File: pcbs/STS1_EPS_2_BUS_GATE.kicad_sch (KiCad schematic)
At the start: 19 parts, among them Q5 SI7135DP-T1-GE3, Q6 2N7002, U13 4082, U3 TPS2420RSAT

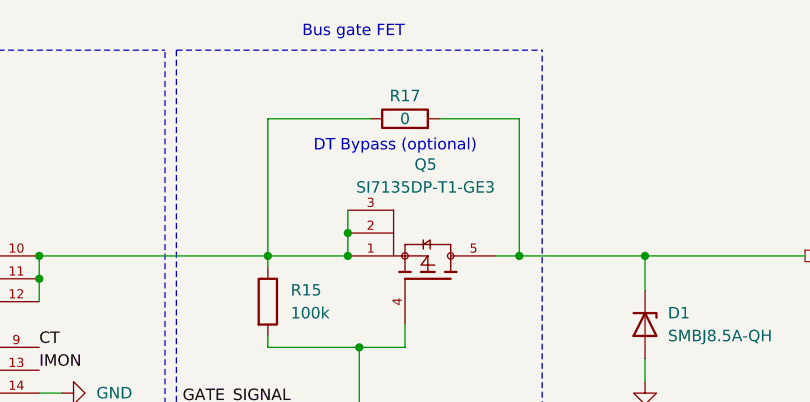
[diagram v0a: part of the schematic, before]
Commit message: Marked optional bypasses as "Do not place".
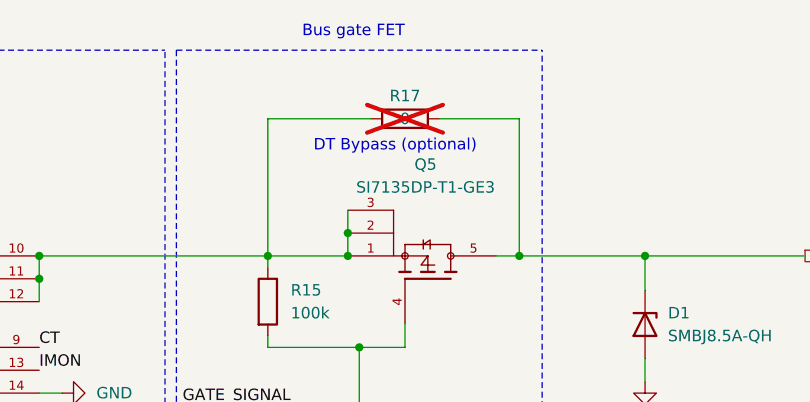
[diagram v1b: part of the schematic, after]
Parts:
- R17: now not fitted
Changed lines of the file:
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@@
 		(in_bom yes)
 		(on_board yes)
-		(dnp no)
+		(dnp yes)
 		(property "Reference" "R17"
 			(at 116.84 21.59 90)

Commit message: Added more part numbers.
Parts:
- C2: Part Nr. (none) -> C0805T105K4RALTU
- R12: Part Nr. (none) -> CPF0805B40K2E1
- R13: Part Nr. (none) -> RN73R2ATTD6342B25
- R14: Part Nr. (none) -> ERA-6ARB3162V
- R15, R20, R21, R22, R23, R24: Part Nr. (none) -> TNPW0805100KFEEA
- R4: Part Nr. (none) -> TNPW0805100RFETA
- U13: Part Nr. (none) -> HEF4082BT-Q100J
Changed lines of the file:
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@@
+			)
+		)
+		(property "Part Nr." "TNPW0805100KFEEA"
+			(at 43.18 182.88 0)
+			(effects
+				(font
+					(size 1.27 1.27)
+				)
+				(hide yes)
 			)
 		)
@@
 			)
 		)
+		(property "Part Nr." ""
+			(at 119.38 41.91 0)
+			(effects
+				(font
+					(size 1.27 1.27)
+				)
+				(hide yes)
+			)
+		)
 		(pin "1"
 		)
@@
 			)
 		)
+		(property "Part Nr." ""
+			(at 166.37 134.62 0)
+			(effects
+				(font
+					(size 1.27 1.27)
+				)
+				(hide yes)
+			)
+		)
 		(pin "1"
 		)
@@
 			)
 		)
+		(property "Part Nr." "TNPW0805100KFEEA"
+			(at 101.6 44.45 0)
+			(effects
+				(font
+					(size 1.27 1.27)
+				)
+				(hide yes)
+			)
+		)
 		(pin "1"
 		)
@@
 			)
 		)
+		(property "Part Nr." ""
+			(at 168.91 129.54 0)
+			(effects
+				(font
+					(size 1.27 1.27)
+				)
+				(hide yes)
+			)
+		)
 		(pin "1"
 		)
@@
 			)
 		)
+		(property "Part Nr." ""
+			(at 143.51 46.99 0)
+			(effects
+				(font
+					(size 1.27 1.27)
+				)
+				(hide yes)
+			)
+		)
 		(pin "1"
 		)
@@
 			)
 		)
+		(property "Part Nr." "CPF0805B40K2E1"
+			(at 43.18 95.25 0)
+			(effects
+				(font
+					(size 1.27 1.27)
+				)
+				(hide yes)
+			)
+		)
 		(pin "1"
 		)
@@
 			)
 		)
+		(property "Part Nr." "HEF4082BT-Q100J"
+			(at 135.89 96.52 0)
+			(effects
+				(font
+					(size 1.27 1.27)
+				)
+				(hide yes)
+			)
+		)
 		(pin "9"
 		)
@@
 			)
 		)
+		(property "Part Nr." "TNPW0805100KFEEA"
+			(at 73.66 139.7 0)
+			(effects
+				(font
+					(size 1.27 1.27)
+				)
+				(hide yes)
+			)
+		)
 		(pin "1"
 		)
@@
 			)
 		)
+		(property "Part Nr." "C0805T105K4RALTU"
+			(at 60.96 95.25 0)
+			(effects
+				(font
+					(size 1.27 1.27)
+				)
+				(hide yes)
+			)
+		)
 		(pin "1"
 		)
@@
 					(size 1.27 1.27)
 				)
+			)
+		)
+		(property "Part Nr." "RN73R2ATTD6342B25"
+			(at 52.07 95.25 0)
+			(effects
+				(font
+					(size 1.27 1.27)
+				)
+				(hide yes)
 			)
 		)
@@
 			)
 		)
+		(property "Part Nr." "HEF4082BT-Q100J"
+			(at 135.89 134.62 0)
+			(effects
+				(font
+					(size 1.27 1.27)
+				)
+				(hide yes)
+			)
+		)
 		(pin "9"
 		)
@@
 			)
 		)
+		(property "Part Nr." "ERA-6ARB3162V"
+			(at 71.12 95.25 0)
+			(effects
+				(font
+					(size 1.27 1.27)
+				)
+				(hide yes)
+			)
+		)
 		(pin "1"
 		)
@@
 			)
 		)
+		(property "Part Nr." ""
+			(at 149.86 134.62 0)
+			(effects
+				(font
+					(size 1.27 1.27)
+				)
+				(hide yes)
+			)
+		)
 		(pin "1"
 		)
@@
 			)
 		)
+		(property "Part Nr." "TNPW0805100RFETA"
+			(at 156.21 134.62 0)
+			(effects
+				(font
+					(size 1.27 1.27)
+				)
+				(hide yes)
+			)
+		)
 		(pin "1"
 		)
@@
 			)
 		)
+		(property "Part Nr." "TNPW0805100KFEEA"
+			(at 43.18 139.7 0)
+			(effects
+				(font
+					(size 1.27 1.27)
+				)
+				(hide yes)
+			)
+		)
 		(pin "1"
 		)
@@
 		)
 		(property "Description" ""
+			(at 43.18 161.29 0)
+			(effects
+				(font
+					(size 1.27 1.27)
+				)
+				(hide yes)
+			)
+		)
+		(property "Part Nr." "TNPW0805100KFEEA"
 			(at 43.18 161.29 0)
 			(effects
@@
 			)
 		)
+		(property "Part Nr." ""
+			(at 116.84 24.13 0)
+			(effects
+				(font
+					(size 1.27 1.27)
+				)
+				(hide yes)
+			)
+		)
 		(pin "1"
 		)
@@
 			)
 		)
+		(property "Part Nr." "TNPW0805100KFEEA"
+			(at 73.66 161.29 0)
+			(effects
+				(font
+					(size 1.27 1.27)
+				)
+				(hide yes)
+			)
+		)
 		(pin "1"
 		)
@@
 				(hide yes)
 			)
+		)
+		(property "Part Nr." ""
+			(at 58.42 52.07 0)
+			(effects
+				(font
+					(size 1.27 1.27)
+				)
+				(hide yes)
+			)

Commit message: Fixed footprint of U3 and U6 on STS1_EPS_2.
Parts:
- U3: footprint Package_DFN_QFN:VQFN-16-1EP_3x3mm_P0.5mm_EP1.45x1.45mm_ThermalVias -> STS_Package_DFN_QFN:QFN65P400X400X100-17N
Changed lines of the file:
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@@
 			)
 		)
-		(property "Footprint" "Package_DFN_QFN:VQFN-16-1EP_3x3mm_P0.5mm_EP1.45x1.45mm_ThermalVias"
+		(property "Footprint" "STS_Package_DFN_QFN:QFN65P400X400X100-17N"
 			(at 58.42 52.07 0)
 			(effects

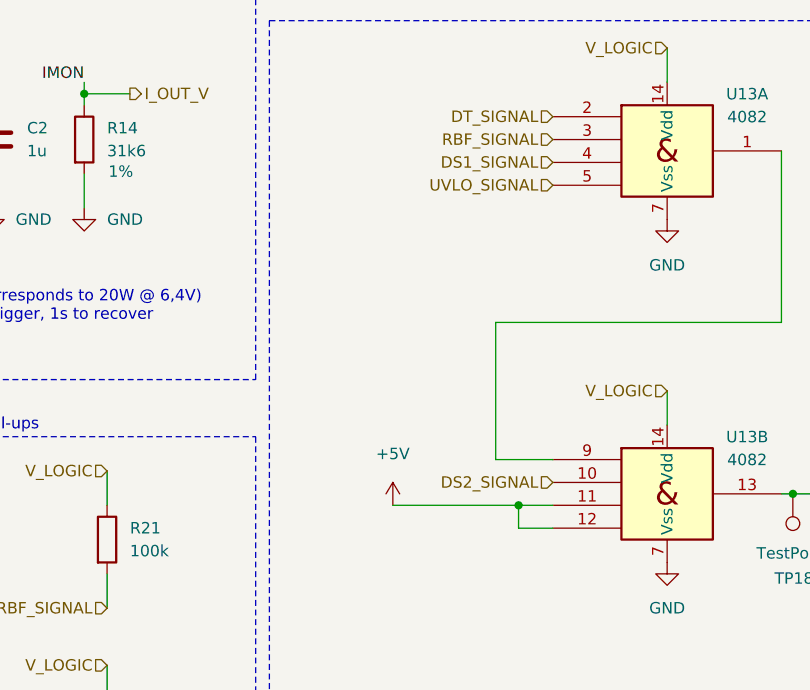
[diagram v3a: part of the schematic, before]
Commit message: Fixed inhibit logic.
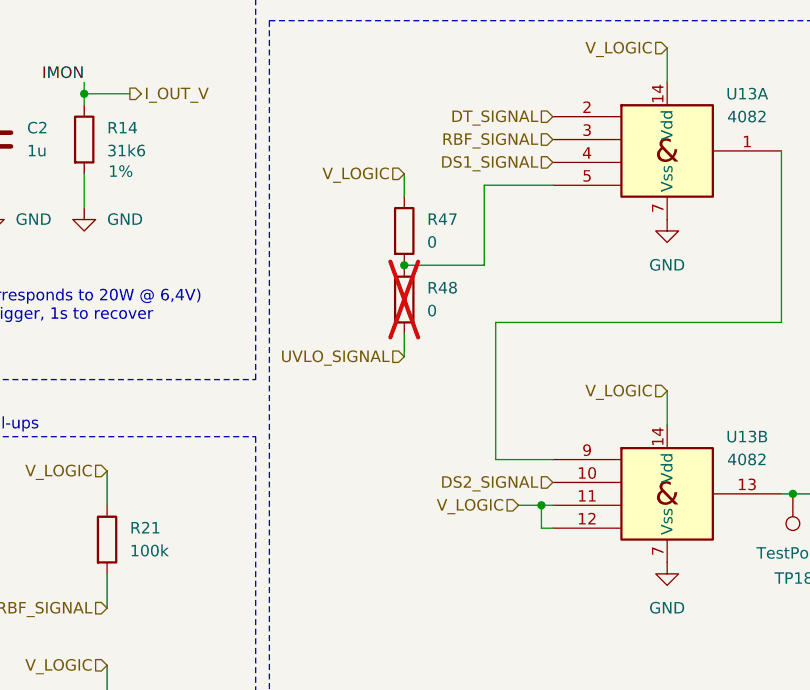
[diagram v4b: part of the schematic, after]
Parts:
- added R47, R48: 0, Resistor_SMD:R_0805_2012Metric, symbol Device:R
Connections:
- net +5V is gone; now on net V_LOGIC: U13.11, U13.12
- net UVLO_SIGNAL: now also R48.2; no longer U13.5
- net V_LOGIC: now also R47.1
- new net: R47.2, R48.1, U13.5
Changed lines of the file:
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@@
 	)
 	(junction
+		(at 121.92 135.89)
+		(diameter 0)
+		(color 0 0 0 0)
+	)
+	(junction
 		(at 71.12 90.17)
 		(diameter 0)
@@
 	)
 	(junction
-		(at 119.38 135.89)
+		(at 106.68 109.22)
 		(diameter 0)
 		(color 0 0 0 0)
@@
 	(wire
 		(pts
+			(xy 115.57 100.33) (xy 115.57 109.22)
+		)
+		(stroke
+			(width 0)
+			(type default)
+		)
+	)
+	(wire
+		(pts
 			(xy 73.66 165.1) (xy 73.66 167.64)
 		)
@@
 	(wire
 		(pts
-			(xy 119.38 135.89) (xy 123.19 135.89)
+			(xy 121.92 135.89) (xy 123.19 135.89)
 		)
 		(stroke
@@
 	(wire
 		(pts
-			(xy 123.19 138.43) (xy 119.38 138.43)
+			(xy 123.19 138.43) (xy 121.92 138.43)
 		)
 		(stroke
@@
 	(wire
 		(pts
-			(xy 119.38 138.43) (xy 119.38 135.89)
+			(xy 121.92 138.43) (xy 121.92 135.89)
 		)
 		(stroke
@@
 	(wire
 		(pts
+			(xy 115.57 109.22) (xy 106.68 109.22)
+		)
+		(stroke
+			(width 0)
+			(type default)
+		)
+	)
+	(wire
+		(pts
 			(xy 168.91 124.46) (xy 168.91 129.54)
 		)
@@
 	(wire
 		(pts
-			(xy 71.12 99.06) (xy 71.12 102.87)
+			(xy 123.19 100.33) (xy 115.57 100.33)
 		)
 		(stroke
@@
 	(wire
 		(pts
-			(xy 43.18 132.08) (xy 43.18 135.89)
+			(xy 71.12 99.06) (xy 71.12 102.87)
 		)
 		(stroke
@@
 		)
 	)
-	(polyline
+	(wire
 		(pts
-			(xy 91.44 16.51) (xy 132.08 16.51)
+			(xy 43.18 132.08) (xy 43.18 135.89)
 		)
 		(stroke
 			(width 0)
-			(type dash)
+			(type default)
 		)
 	)
-	(wire
+	(polyline
 		(pts
-			(xy 101.6 39.37) (xy 101.6 40.64)
+			(xy 91.44 16.51) (xy 132.08 16.51)
 		)
 		(stroke
 			(width 0)
-			(type default)
+			(type dash)
 		)
 	)
 	(wire
 		(pts
-			(xy 105.41 135.89) (xy 119.38 135.89)
+			(xy 101.6 39.37) (xy 101.6 40.64)
 		)
 		(stroke
@@
 	(wire
 		(pts
+			(xy 106.68 99.06) (xy 106.68 101.6)
+		)
+		(stroke
+			(width 0)
+			(type default)
+		)
+	)
+	(wire
+		(pts
 			(xy 110.49 39.37) (xy 110.49 36.83)
 		)
@@
 	(wire
 		(pts
+			(xy 119.38 135.89) (xy 121.92 135.89)
+		)
+		(stroke
+			(width 0)
+			(type default)
+		)
+	)
+	(wire
+		(pts
 			(xy 52.07 99.06) (xy 52.07 102.87)
 		)
@@
 	(wire
 		(pts
+			(xy 106.68 119.38) (xy 106.68 116.84)
+		)
+		(stroke
+			(width 0)
+			(type default)
+		)
+	)
+	(wire
+		(pts
 			(xy 101.6 49.53) (xy 111.76 49.53)
 		)
@@
 	(hierarchical_label "V_LOGIC"
 		(shape input)
+		(at 119.38 135.89 180)
+		(fields_autoplaced yes)
+		(effects
+			(font
+				(size 1.27 1.27)
+			)
+			(justify right)
+		)
+	)
+	(hierarchical_label "V_LOGIC"
+		(shape input)
 		(at 73.66 153.67 180)
 		(fields_autoplaced yes)
@@
 	(hierarchical_label "V_LOGIC"
 		(shape input)
+		(at 106.68 99.06 180)
+		(fields_autoplaced yes)
+		(effects
+			(font
+				(size 1.27 1.27)
+			)
+			(justify right)
+		)
+	)
+	(hierarchical_label "V_LOGIC"
+		(shape input)
 		(at 135.89 123.19 180)
 		(fields_autoplaced yes)
@@
 	(hierarchical_label "UVLO_SIGNAL"
 		(shape input)
-		(at 123.19 100.33 180)
+		(at 106.68 119.38 180)
 		(fields_autoplaced yes)
 		(effects
@@
 	(symbol
 		(lib_id "Device:R")
+		(at 106.68 113.03 0)
+		(unit 1)
+		(exclude_from_sim no)
+		(in_bom yes)
+		(on_board yes)
+		(dnp yes)
+		(fields_autoplaced yes)
+		(property "Reference" "R48"
+			(at 109.22 111.7599 0)
+			(effects
+				(font
+					(size 1.27 1.27)
+				)
+				(justify left)
+			)
+		)
+		(property "Value" "0"
+			(at 109.22 114.2999 0)
+			(effects
+				(font
+					(size 1.27 1.27)
+				)
+				(justify left)
+			)
+		)
+		(property "Footprint" "Resistor_SMD:R_0805_2012Metric"
+			(at 104.902 113.03 90)
+			(effects
+				(font
+					(size 1.27 1.27)
+				)
+				(hide yes)
+			)
+		)
+		(property "Datasheet" "~"
+			(at 106.68 113.03 0)
+			(effects
+				(font
+					(size 1.27 1.27)
+				)
+				(hide yes)
+			)
+		)
+		(property "Description" "Resistor"
+			(at 106.68 113.03 0)
+			(effects
+				(font
+					(size 1.27 1.27)
+				)
+				(hide yes)
+			)
+		)
+		(pin "1"
+		)
+		(pin "2"
+		)
+		(instances
+			(project "STS1_EPS_2"
+				(path "/38c03ff7-ea47-4d00-b37d-ddcaa7d87722/4a4cf4f3-b3ca-46d9-b2ff-f21a8c4df335"
+					(reference "R48")
+					(unit 1)
+				)
+			)
+		)
+	)
+	(symbol
+		(lib_id "Device:R")
 		(at 73.66 139.7 0)
 		(unit 1)
@@
 	)
 	(symbol
-		(lib_id "power:+5V")
-		(at 105.41 135.89 0)
-		(unit 1)
-		(exclude_from_sim no)
-		(in_bom yes)
-		(on_board yes)
-		(dnp no)
-		(property "Reference" "#PWR0135"
-			(at 105.41 139.7 0)
-			(effects
-				(font
-					(size 1.27 1.27)
-				)
-				(hide yes)
-			)
-		)
-		(property "Value" "+5V"
-			(at 105.41 130.175 0)
-			(effects
-				(font
-					(size 1.27 1.27)
-				)
-			)
-		)
-		(property "Footprint" ""
-			(at 105.41 135.89 0)
-			(effects
-				(font
-					(size 1.27 1.27)
-				)
-				(hide yes)
-			)
-		)
-		(property "Datasheet" ""
-			(at 105.41 135.89 0)
-			(effects
-				(font
-					(size 1.27 1.27)
-				)
-				(hide yes)
-			)
-		)
-		(property "Description" "Power symbol creates a global label with name \"+5V\""
-			(at 105.41 135.89 0)
-			(effects
-				(font
-					(size 1.27 1.27)
-				)
-				(hide yes)
-			)
-		)
-		(pin "1"
-		)
-		(instances
-			(project "STS1_EPS_2"
-				(path "/38c03ff7-ea47-4d00-b37d-ddcaa7d87722/4a4cf4f3-b3ca-46d9-b2ff-f21a8c4df335"
-					(reference "#PWR0135")
-					(unit 1)
-				)
-			)
-		)
-	)
-	(symbol
 		(lib_id "power:GND")
 		(at 40.64 64.77 270)
@@
 					(unit 1)
 				)
+			)
+		)
+	)
+	(symbol
+		(lib_id "Device:R")
+		(at 106.68 105.41 0)
+		(unit 1)
+		(exclude_from_sim no)
+		(in_bom yes)
+		(on_board yes)
+		(dnp no)
+		(fields_autoplaced yes)
+		(property "Reference" "R47"
+			(at 109.22 104.1399 0)
+			(effects
+				(font
+					(size 1.27 1.27)
+				)
+				(justify left)
+			)
+		)
+		(property "Value" "0"
+			(at 109.22 106.6799 0)
+			(effects
+				(font
+					(size 1.27 1.27)
+				)
+				(justify left)
+			)
+		)
+		(property "Footprint" "Resistor_SMD:R_0805_2012Metric"
+			(at 104.902 105.41 90)
+			(effects
+				(font
+					(size 1.27 1.27)
+				)
+				(hide yes)
+			)
+		)
+		(property "Datasheet" "~"
+			(at 106.68 105.41 0)
+			(effects
+				(font
+					(size 1.27 1.27)
+				)
+				(hide yes)
+			)
+		)
+		(property "Description" "Resistor"
+			(at 106.68 105.41 0)
+			(effects
+				(font
+					(size 1.27 1.27)
+				)
+				(hide yes)
+			)
+		)
+		(pin "1"
+		)
+		(pin "2"
+		)
+		(instances
+			(project "STS1_EPS_2"
+				(path "/38c03ff7-ea47-4d00-b37d-ddcaa7d87722/4a4cf4f3-b3ca-46d9-b2ff-f21a8c4df335"
+					(reference "R47")
+					(unit 1)
+				)

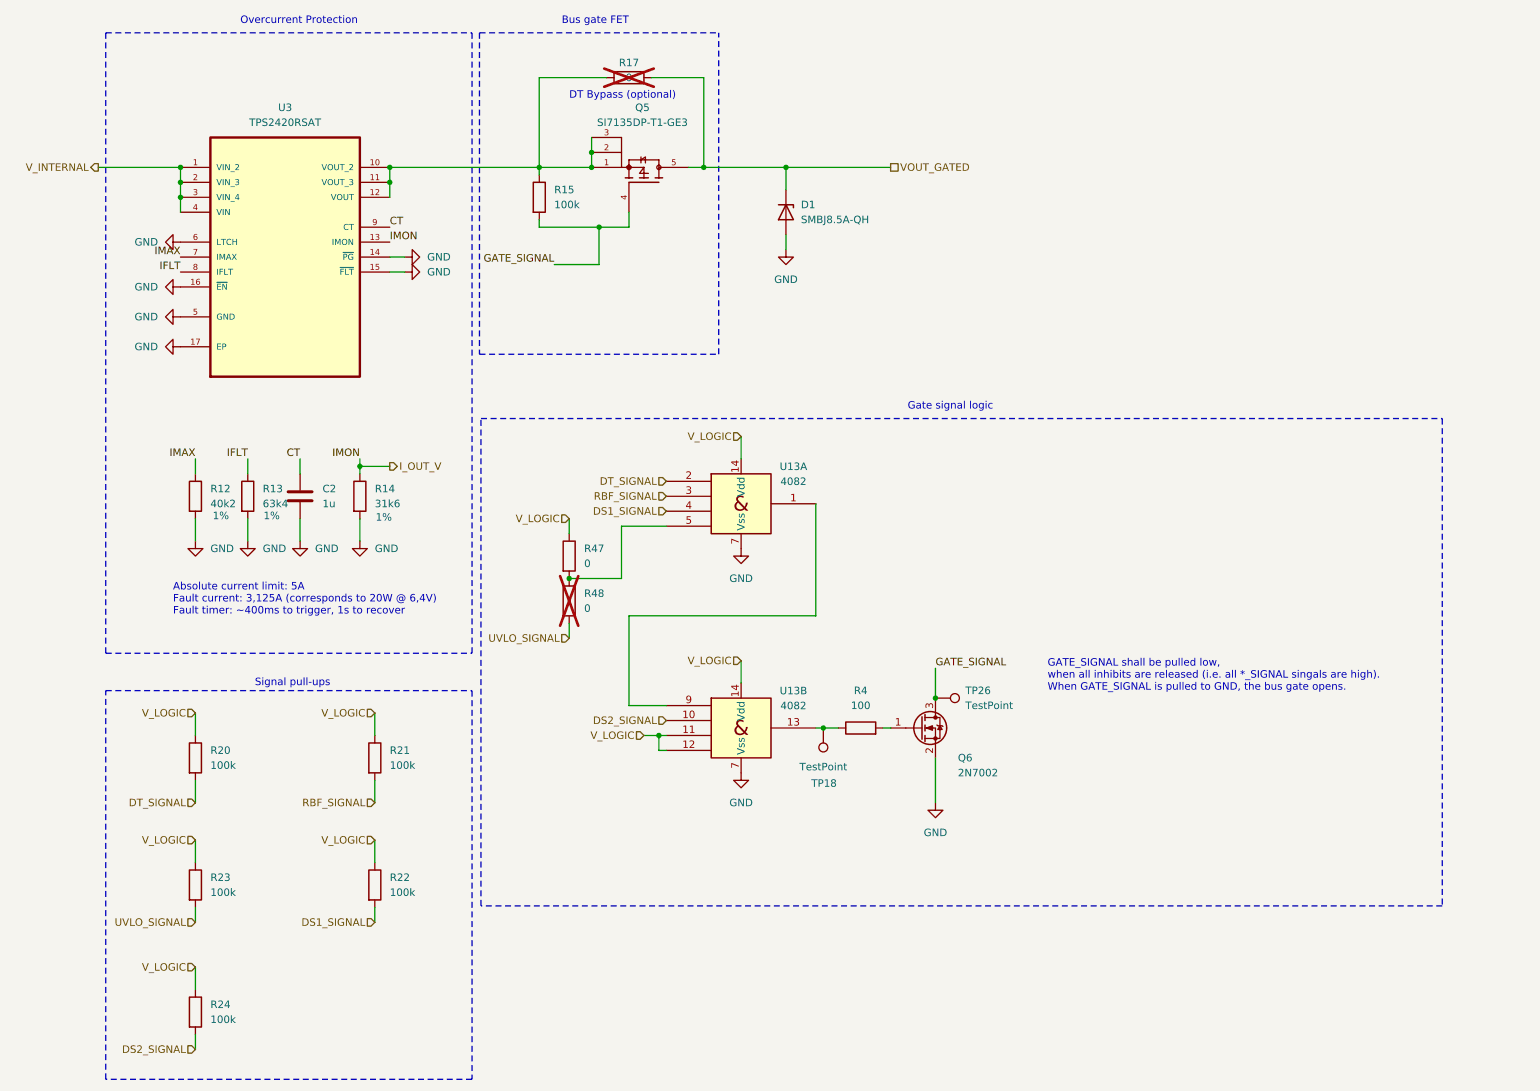
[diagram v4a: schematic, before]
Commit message: feat(EPS PCB 2): start redesign & cleanup for less idle power consumption
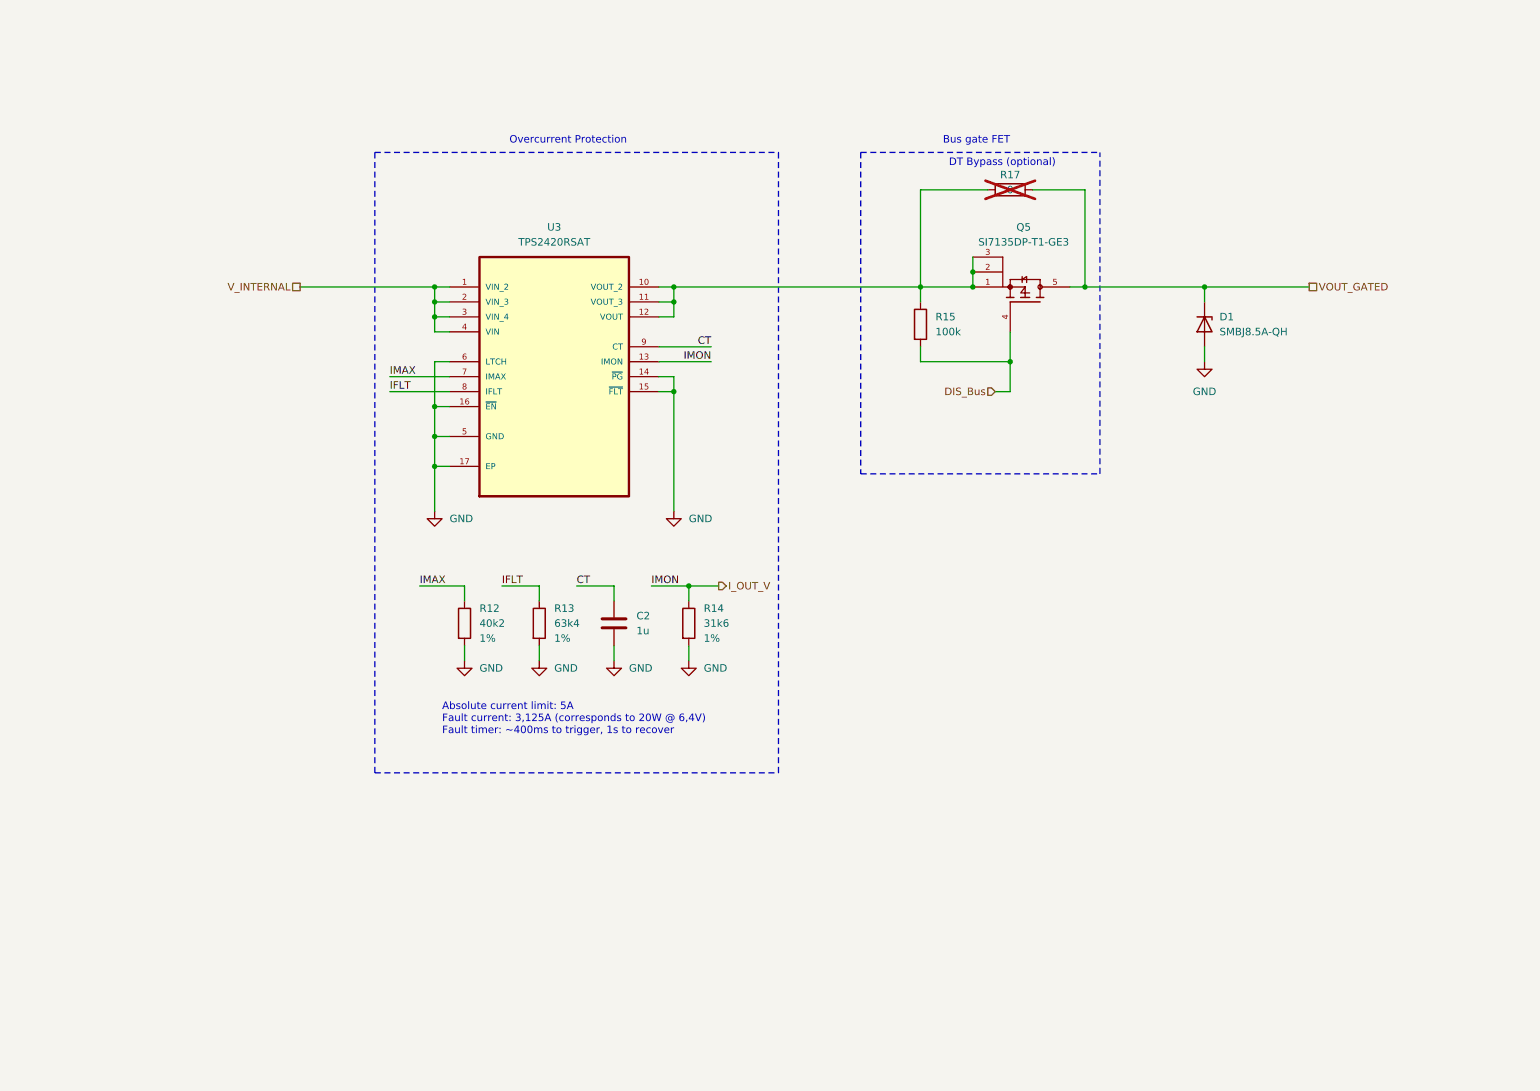
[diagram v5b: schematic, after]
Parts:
- removed Q6: 2N7002, Package_TO_SOT_SMD:SOT-23, symbol Transistor_FET:2N7002
- removed R20, R21, R22, R23, R24: 100k, Resistor_SMD:R_0805_2012Metric, symbol Device:R
- removed R4: 100, Resistor_SMD:R_0805_2012Metric, symbol Device:R
- removed R47, R48: 0, Resistor_SMD:R_0805_2012Metric, symbol Device:R
- removed TP18, TP26: TestPoint, TestPoint:TestPoint_THTPad_D1.0mm_Drill0.5mm, symbol Connector:TestPoint
- removed U13: 4082, Package_SO:SOIC-14_3.9x8.7mm_P1.27mm, symbol 4xxx_IEEE:4082
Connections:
- net GATE_SIGNAL renamed DIS_Bus
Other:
- note removed: "GATE_SIGNAL shall be pulled low, when all inhibits are released (i.e. all *_SIGNAL singals are high). When GATE_SIGNAL is pulled to GND, the bus gate opens."
- note removed: "Gate signal logic"
- note removed: "Signal pull-ups"
- moved on the sheet: C2, D1, Q5, R12, R13, R14, R15, R17, U3
